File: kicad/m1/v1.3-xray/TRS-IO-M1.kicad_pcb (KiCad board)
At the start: 2 copper layers, 111.9 x 94 mm, 34 parts, among them J1 Conn_02x20_Odd_Even, J2 Conn_02x20_Odd_Even, J3 SD_Card, J4 Conn_01x02_Male, J5 Conn_01x02_Male, J6 DB15_Female_HighDensity, Q1 2N7000, Q2 2N7000, SW1 SW_Push, U1 HiLetgo-ESP-32S, U2 Artix-7-15T, U3 74LVC245, U4 74LVC245, U5 74LVC245, U6 74LVC245, U7 MCP43x1

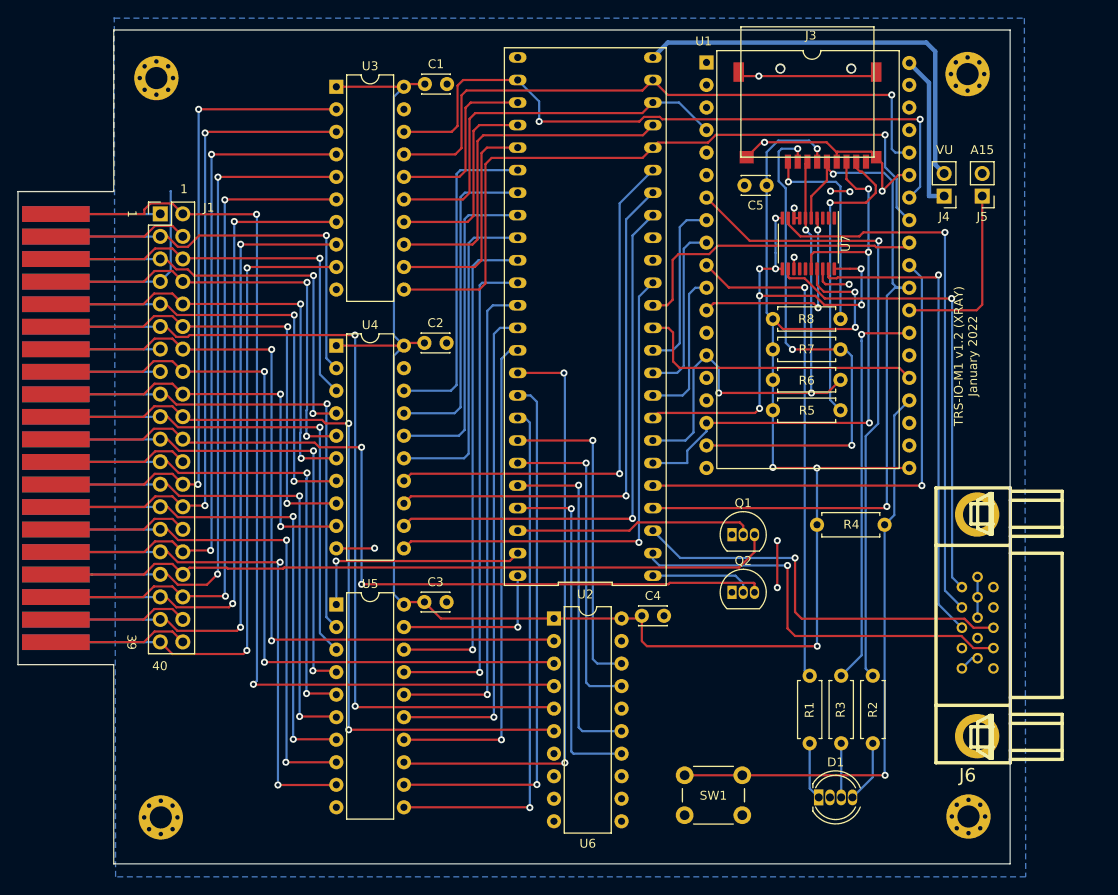
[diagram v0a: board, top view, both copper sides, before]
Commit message: PCB for TRS-IO-XRAY 1.3 (Nano 9K)
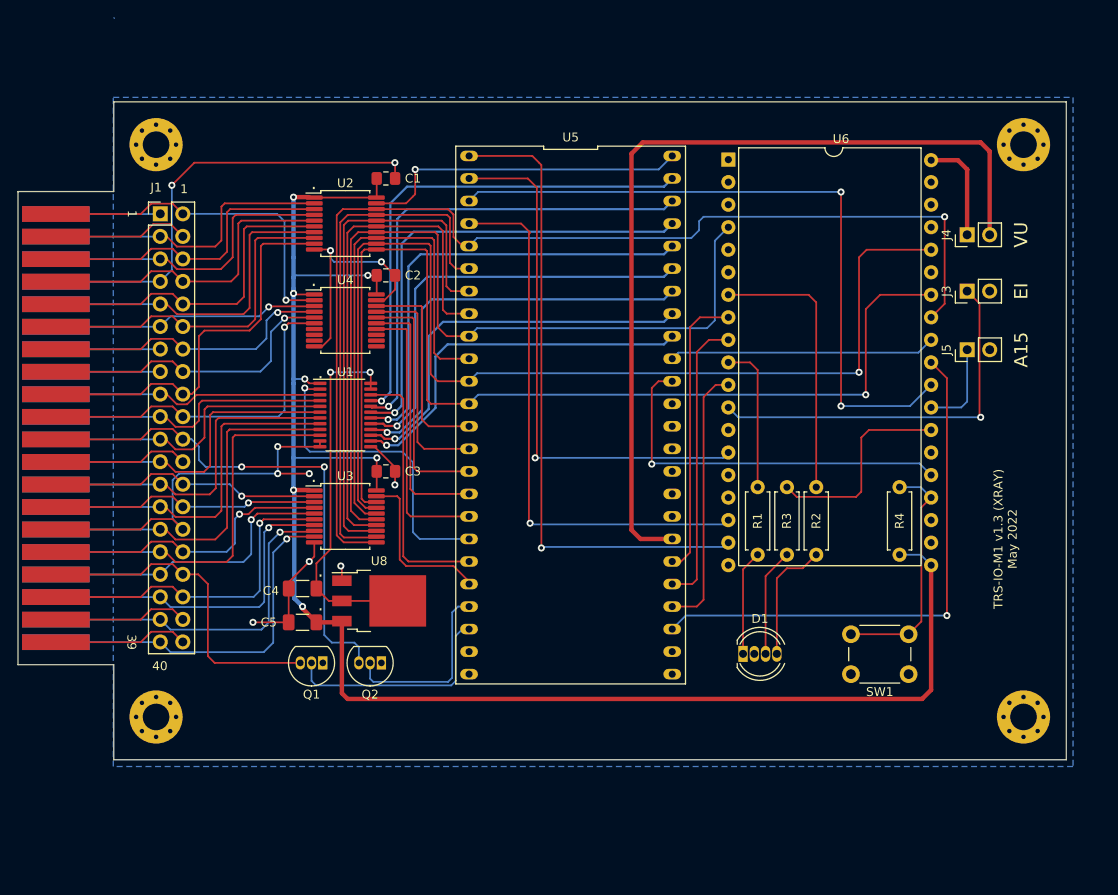
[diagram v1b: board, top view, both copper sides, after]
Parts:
- removed J6: DB15_Female_HighDensity, TRS-IO-M1:DB_15F-VGA
- removed R5, R6, R7, R8: 10K, Resistor_THT:R_Axial_DIN0207_L6.3mm_D2.5mm_P7.62mm_Horizontal
- removed U7: MCP43x1, Package_SO:TSSOP-20_4.4x6.5mm_P0.65mm
- added U8: LD1117DT18TR, Package_TO_SOT_SMD:TO-252-3_TabPin2, F.Cu at (143.5, 112.4)
- C1, C2, C3: footprint Capacitor_THT:C_Disc_D3.0mm_W2.0mm_P2.50mm -> Capacitor_SMD:C_0805_2012Metric_Pad1.18x1.45mm_HandSolder
- C4: value 0.1uF -> 10u; footprint Capacitor_THT:C_Disc_D3.0mm_W2.0mm_P2.50mm -> Capacitor_SMD:C_1206_3216Metric_Pad1.33x1.80mm_HandSolder
- C5: value 0.1uF -> 100u; footprint Capacitor_THT:C_Disc_D3.0mm_W2.0mm_P2.50mm -> Capacitor_SMD:C_1206_3216Metric_Pad1.33x1.80mm_HandSolder
- H1, H2, H3, H4: footprint MountingHole:MountingHole_2.5mm_Pad_Via -> MountingHole:MountingHole_3mm_Pad_Via
- J3: value SD_Card -> Conn_01x02_Male; footprint TRS-IO-M1:TFP09-2-12B -> Connector_PinHeader_2.54mm:PinHeader_1x02_P2.54mm_Vertical
- U1: value HiLetgo-ESP-32S -> SN74LVCH8T245; footprint TRS-IO-M1:DIP-38_W22.9mm -> Package_SO:TSSOP-24_4.4x7.8mm_P0.65mm
- U2: value Artix-7-15T -> 74LVC245; footprint TRS-IO-M1:DIP-48_600_ELL -> Package_SO:SSOP-20_5.3x7.2mm_P0.65mm
- U3, U4: footprint Package_DIP:DIP-20_W7.62mm -> Package_SO:SSOP-20_5.3x7.2mm_P0.65mm
- U5: value 74LVC245 -> Tango_Nano_9K; footprint Package_DIP:DIP-20_W7.62mm -> TRS-IO-M1:DIP-48_W22.9mm
- U6: value 74LVC245 -> HiLetgo-ESP-32S; footprint Package_DIP:DIP-20_W7.62mm -> TRS-IO-M1:DIP-38_W22.9mm
- moved C5 71.9 mm to (134.9, 114.8)
- moved U1 56.9 mm to (139.7, 91.4)
- moved U6 55.3 mm to (182.9, 62.6)
- moved U3 48.4 mm to (139.7, 102.9)
- moved Q1 48.3 mm to (137.2, 119.4), turned to 180 degrees
- moved Q2 40.3 mm to (143.8, 119.4), turned to 180 degrees
- moved C4 38.4 mm to (134.9, 111.0), turned to 180 degrees
- moved U5 34.0 mm to (165.1, 91.4), turned to -90 degrees
- moved J3 30.9 mm to (209.8, 77.5), turned to 90 degrees
- moved U2 29.0 mm to (139.7, 69.8), turned to 0 degrees
- moved SW1 24.6 mm to (203.2, 120.7)
- moved R2 22.2 mm to (192.8, 99.6)
- moved R3 22.1 mm to (189.5, 99.6)
- moved R1 22.1 mm to (186.2, 99.6)
- moved D1 18.3 mm to (184.5, 118.4)
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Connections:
- C4 pad 1: +3V3 -> +1V8
- J3 pad 1: Net-(J3-Pad1) -> EI
- J3 pad 2: CS_SD_CARD -> GND
- U1 pad 1: unconnected-(U1-Pad1) -> +3V3
- U1 pad 10: LED_RED -> D2
- U1 pad 11: ESP_S2 -> GND
- U1 pad 12: CS_MCP43x1 -> GND
- U1 pad 14: MOSI -> DD2
- U1 pad 15: unconnected-(U1-Pad15) -> DD0
- U1 pad 16: unconnected-(U1-Pad16) -> DD5
- U1 pad 17: MISO -> DD3
- U1 pad 18: CS_SD_CARD -> DD6
- U1 pad 19: GND -> DD1
- U1 pad 2: unconnected-(U1-Pad2) -> READ_N
- U1 pad 20: +3V3 -> DD7
- U1 pad 21: unconnected-(U1-Pad21) -> DD4
- U1 pad 22: unconnected-(U1-Pad22) -> DBUS_SEL_N
- U1 pad 23: BUTTON -> +1V8
- U1 pad 24: REQ -> +1V8
- U1 pad 3: unconnected-(U1-Pad3) -> D4
- U1 pad 4: AA3 -> D7
- U1 pad 5: unconnected-(U1-Pad5) -> D1
- U1 pad 6: unconnected-(U1-Pad6) -> D6
- U1 pad 7: LED_GREEN -> D3
- U1 pad 8: ESP_S0 -> D5
- U1 pad 9: ESP_S1 -> D0
- U2 pad 1: INT -> +3V3
- U2 pad 10: ESP_S1 -> GND
- U2 pad 11: ESP_S0 -> AA0_9
- U2 pad 12: REQ -> AA1_8
- U2 pad 13: DONE -> AA4_14
- U2 pad 14: AA9 -> AA3_11
- U2 pad 15: unconnected-(U2-Pad15) -> AA5_15
- U2 pad 16: unconnected-(U2-Pad16) -> AA7_13
- U2 pad 17: AA8 -> AA6_12
- U2 pad 18: AA14 -> AA2_10
- U2 pad 19: AA11 -> A1_MUX
- U2 pad 2: VGA_VSYNC -> A10
- U2 pad 20: AA2 -> +3V3
- U2 pad 3: VGA_HSYNC -> A12
- U2 pad 4: SCK -> A13
- U2 pad 5: CS_FPGA -> A15
- U2 pad 6: MISO -> A11
- U2 pad 7: MOSI -> A14
- U2 pad 8: VGA_RGB -> A8
- U2 pad 9: ESP_S2 -> A9
- U3 pad 11: AA2 -> AA2_10
- U3 pad 12: AA6 -> AA6_12
- U3 pad 13: AA7 -> AA7_13
- U3 pad 14: AA5 -> AA5_15
- U3 pad 15: AA3 -> AA3_11
- U3 pad 16: AA4 -> AA4_14
- U3 pad 17: AA1 -> AA1_8
- U3 pad 18: AA0 -> AA0_9
- U3 pad 19: GND -> A0_MUX
- U4 pad 11: AA9 -> unconnected-(U4-Pad11)
- U4 pad 12: AA8 -> unconnected-(U4-Pad12)
- U4 pad 13: AA14 -> unconnected-(U4-Pad13)
- U4 pad 14: AA11 -> Z80_IN_N
- U4 pad 15: AA15 -> Z80_RD_N
- U4 pad 16: AA13 -> Z80_WR_N
- U4 pad 17: AA12 -> Z80_OUT_N
- U4 pad 18: AA10 -> Z80_RAS_N
- U4 pad 2: A10 -> RAS_N
- U4 pad 3: A12 -> OUT_N
- U4 pad 4: A13 -> WR_N
- U4 pad 5: A15 -> RD_N
- U4 pad 6: A11 -> IN_N
- U4 pad 7: A14 -> unconnected-(U4-Pad7)
- U4 pad 8: A8 -> unconnected-(U4-Pad8)
- U4 pad 9: A9 -> unconnected-(U4-Pad9)
- U5 pad 1: READ_N -> CS_SD_CARD
- U5 pad 10: GND -> AA4_14
- U5 pad 11: DD2 -> AA1_8
- U5 pad 12: DD0 -> AA0_9
- U5 pad 13: DD5 -> Z80_RAS_N
- U5 pad 14: DD3 -> Z80_OUT_N
- U5 pad 15: DD6 -> Z80_WR_N
- U5 pad 16: DD1 -> Z80_RD_N
- U5 pad 17: DD7 -> Z80_IN_N
- U5 pad 18: DD4 -> READ_N
- U5 pad 2: D4 -> MOSI
- U5 pad 20: +3V3 -> A0_MUX
- U5 pad 3: D7 -> SCK
- U5 pad 4: D1 -> MISO
- U5 pad 5: D6 -> AA2_10
- U5 pad 6: D3 -> AA6_12
- U5 pad 7: D5 -> AA7_13
- U5 pad 8: D0 -> AA5_15
- U5 pad 9: D2 -> AA3_11
- U6 pad 1: +3V3 -> unconnected-(U6-Pad1)
- U6 pad 10: GND -> LED_RED
- U6 pad 11: unconnected-(U6-Pad11) -> ESP_S2
- U6 pad 12: unconnected-(U6-Pad12) -> EI
- U6 pad 13: unconnected-(U6-Pad13) -> GND
- U6 pad 14: Z80_IN_N -> MOSI
- U6 pad 15: Z80_OUT_N -> unconnected-(U6-Pad15)
- U6 pad 16: Z80_RAS_N -> unconnected-(U6-Pad16)
- U6 pad 17: Z80_RD_N -> MISO
- U6 pad 18: Z80_WR_N -> CS_SD_CARD
- U6 pad 2: WR_N -> unconnected-(U6-Pad2)
- U6 pad 3: RD_N -> unconnected-(U6-Pad3)
- U6 pad 4: RAS_N -> AA3_11
- U6 pad 5: OUT_N -> unconnected-(U6-Pad5)
- U6 pad 6: IN_N -> unconnected-(U6-Pad6)
- U6 pad 7: unconnected-(U6-Pad7) -> LED_GREEN
- U6 pad 8: unconnected-(U6-Pad8) -> ESP_S0
- U6 pad 9: unconnected-(U6-Pad9) -> ESP_S1
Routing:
- net AA2_10: track 0.00 -> 126.9 mm, vias 0 -> 1
- net AA1_8: track 0.00 -> 124.2 mm, vias 0 -> 1
- net AA0_9: track 0.00 -> 121.7 mm, vias 0 -> 1
- net AA3_11: track 0.00 -> 98.1 mm
- net AA2: track 80.1 -> 0.00 mm, vias 1 -> 0
- net AA0: track 76.2 -> 0.00 mm, vias 2 -> 0
- net RAS_N: track 111.1 -> 39.2 mm, vias 2 -> 1
- net AA1: track 70.9 -> 0.00 mm, vias 1 -> 0
- net OUT_N: track 98.7 -> 30.1 mm, vias 2 -> 1
- net POT_VGA_GREEN: track 62.2 -> 0.00 mm, vias 1 -> 0
- net AA8: track 61.3 -> 0.00 mm, vias 1 -> 0
- net AA14: track 60.8 -> 0.00 mm, vias 1 -> 0
- net AA11: track 60.4 -> 0.00 mm, vias 1 -> 0
- net AA6_12: track 0.00 -> 60.0 mm
- net AA7_13: track 0.00 -> 59.5 mm
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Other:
- board size 111.9 x 94 mm -> 118.2 x 74.2 mm
- board text added: "."
- board text added: "EI"
- board text added: "TRS-IO-M1 v1.3 (XRAY) May 2022"
- board text removed: "TRS-IO-M1 v1.2 (XRAY) January 2022"

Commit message: PCB updates for TRS-IO-M1 1.3
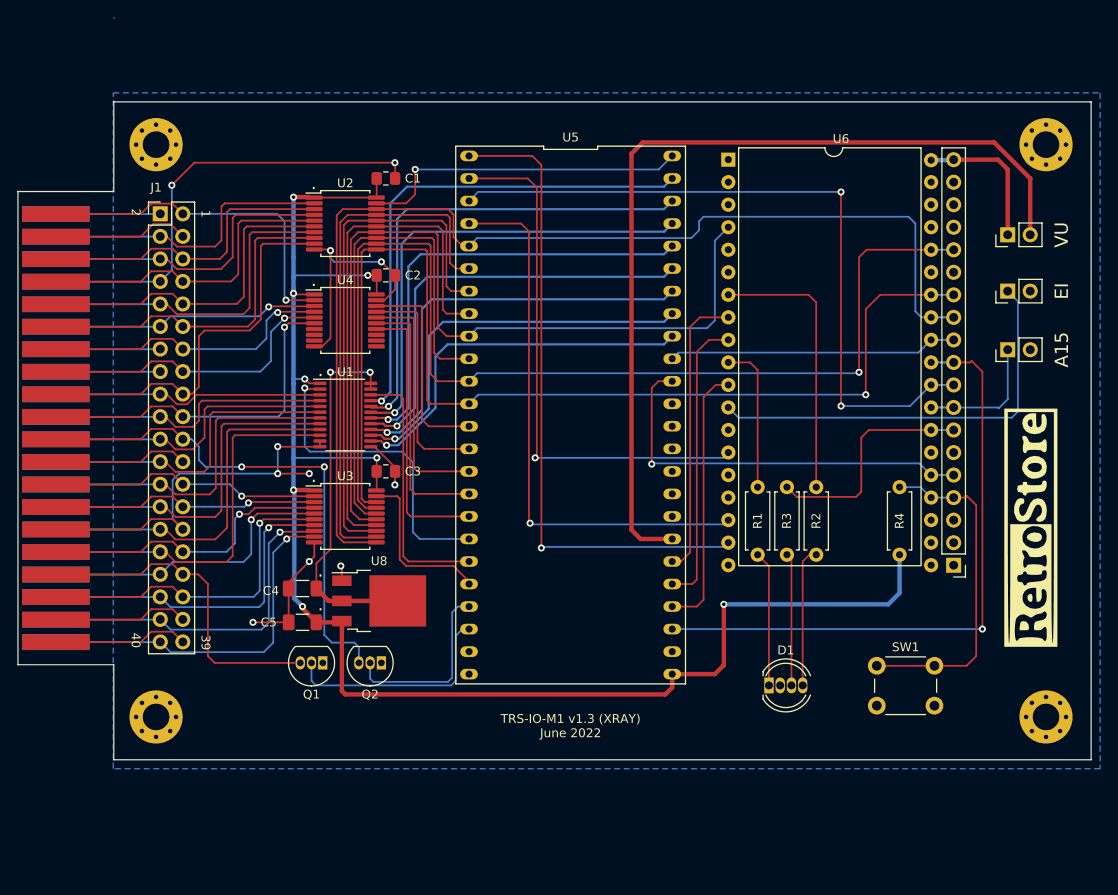
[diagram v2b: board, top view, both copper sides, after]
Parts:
- added G1: LOGO, LOGO, F.Cu at (216.9, 104.1)
- added J6: Conn_01x19, Connector_PinHeader_2.54mm:PinHeader_1x19_P2.54mm_Vertical, F.Cu at (208.3, 108.4)
- moved SW1 4.60 mm to (206.1, 124.2)
- moved D1 4.60 mm to (187.5, 121.9)
- moved J3 4.57 mm to (214.4, 77.5)
- moved J4 4.57 mm to (214.4, 71.1)
- moved J5 4.57 mm to (214.4, 84.1)
- moved H2 2.54 mm to (218.7, 61.0)
- moved H4 2.54 mm to (218.7, 125.5)
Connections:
- U5 pad 25: unconnected-(U5-Pad25) -> +3V3
- U6 pad 20: +3V3 -> unconnected-(U6-Pad20)
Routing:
- net BUTTON: track 27.0 -> 38.3 mm
- net CS_FPGA: track 60.9 -> 70.3 mm
- net +3V3: track 188.3 -> 179.8 mm, vias 7 -> 8
- net +5V: track 11.9 -> 16.5 mm
- net FULL_ADDR: track 10.2 -> 14.7 mm
- net EI: track 43.8 -> 47.5 mm, vias 1 -> 0
- net Net-(D1-Pad1): track 11.9 -> 15.3 mm
- net VU: track 98.2 -> 101.0 mm
- net Net-(D1-Pad3): track 12.2 -> 14.9 mm
- net LED_BLUE: track 23.4 -> 25.9 mm
- net DONE: track 30.1 -> 32.6 mm
- net REQ: track 43.3 -> 45.8 mm
- net SCK: track 77.6 -> 80.2 mm
- net AA1_8: track 124.2 -> 126.8 mm
- net AA0_9: track 121.7 -> 124.3 mm
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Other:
- board size 118.2 x 74.2 mm -> 121 x 74.2 mm
- board text added: "2"
- board text added: "TRS-IO-M1 v1.3 (XRAY) June 2022"
- board text removed: "TRS-IO-M1 v1.3 (XRAY) May 2022"
